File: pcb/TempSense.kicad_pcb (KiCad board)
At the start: 2 copper layers, 90 x 40 mm, 6 parts, among them SW1 Slide_Switch_DPDT_ON-ON_0.3A/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, U1 DC-DC_Converter_Step-Down_5V_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, U2 NodeMCU_Lua_based_ESP8266, U3 Waterproof_Temperature_Sensor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

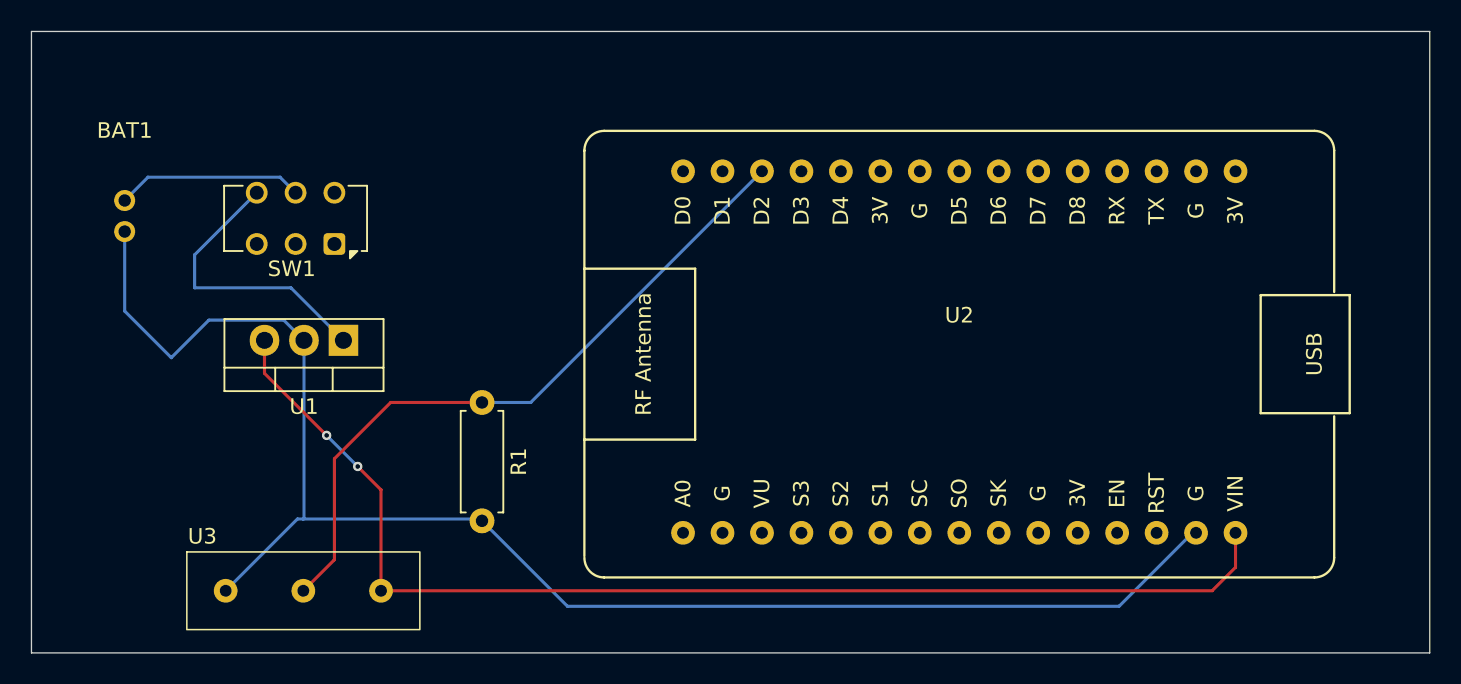
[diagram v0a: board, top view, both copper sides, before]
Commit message: resistor connection corrected to 5V
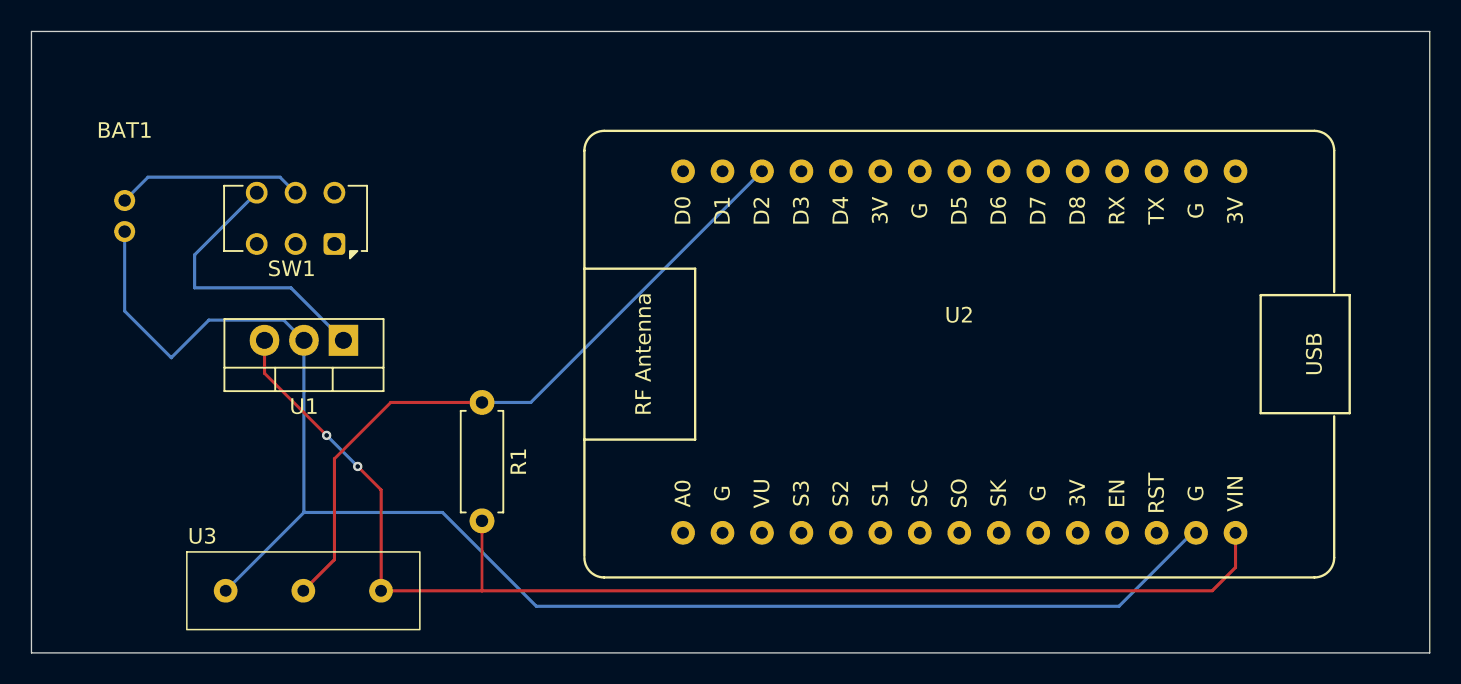
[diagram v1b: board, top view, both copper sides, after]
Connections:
- R1 pad 2: GND -> +5V
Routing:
- net +5V: track 77.1 -> 82.2 mm
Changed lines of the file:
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@@
 			(layers "*.Cu" "*.Mask")
 			(remove_unused_layers no)
-			(net 1 "GND")
+			(net 9 "+5V")
 			(pintype "passive")
 		)
@@
 		(fp_arc
 			(start 14.371974 22.86)
-			(mid 13.999994 23.758021)
+			(mid 13.999993 23.758018)
 			(end 13.101974 24.13)
 			(stroke
@@
 	)
 	(segment
-		(start 105 68.5)
-		(end 104.5 68.5)
+		(start 150.73 69.27)
+		(end 150.96 69.27)
 		(width 0.2)
 		(layer "B.Cu")
@@
 	)
 	(segment
-		(start 105 68.5)
-		(end 110.5 74)
+		(start 93.54 67.96)
+		(end 88.5 73)
+		(width 0.2)
+		(layer "B.Cu")
+		(net 1)
+	)
+	(segment
+		(start 108.5 74)
+		(end 146 74)
+		(width 0.2)
+		(layer "B.Cu")
+		(net 1)
+	)
+	(segment
+		(start 102.46 67.96)
+		(end 108.5 74)
+		(width 0.2)
+		(layer "B.Cu")
+		(net 1)
+	)
+	(segment
+		(start 85 58)
+		(end 87.42 55.58)
+		(width 0.2)
+		(layer "B.Cu")
+		(net 1)
+	)
+	(segment
+		(start 82 55)
+		(end 85 58)
+		(width 0.2)
+		(layer "B.Cu")
+		(net 1)
+	)
+	(segment
+		(start 93.54 67.96)
+		(end 102.46 67.96)
+		(width 0.2)
+		(layer "B.Cu")
+		(net 1)
+	)
+	(segment
+		(start 93.54 56.88)
+		(end 93.54 67.96)
+		(width 0.2)
+		(layer "B.Cu")
+		(net 1)
+	)
+	(segment
+		(start 92.24 55.58)
+		(end 93.54 56.88)
 		(width 0.2)
 		(layer "B.Cu")
@@
 	)
 	(segment
-		(start 85 58)
-		(end 87.42 55.58)
-		(width 0.2)
-		(layer "B.Cu")
-		(net 1)
-	)
-	(segment
-		(start 82 55)
-		(end 85 58)
-		(width 0.2)
-		(layer "B.Cu")
-		(net 1)
-	)
-	(segment
-		(start 110.5 74)
-		(end 146 74)
-		(width 0.2)
-		(layer "B.Cu")
-		(net 1)
-	)
-	(segment
-		(start 104.5 68.5)
-		(end 104.38 68.38)
-		(width 0.2)
-		(layer "B.Cu")
-		(net 1)
-	)
-	(segment
-		(start 93.5 68.38)
-		(end 93.12 68.38)
-		(width 0.2)
-		(layer "B.Cu")
-		(net 1)
-	)
-	(segment
-		(start 92.24 55.58)
-		(end 93.54 56.88)
-		(width 0.2)
-		(layer "B.Cu")
-		(net 1)
-	)
-	(segment
-		(start 104.38 68.38)
-		(end 93.5 68.38)
-		(width 0.2)
-		(layer "B.Cu")
-		(net 1)
-	)
-	(segment
-		(start 93.12 68.38)
-		(end 88.5 73)
-		(width 0.2)
-		(layer "B.Cu")
-		(net 1)
-	)
-	(segment
-		(start 150.73 69.27)
-		(end 150.96 69.27)
-		(width 0.2)
-		(layer "B.Cu")
-		(net 1)
-	)
-	(segment
-		(start 93.54 56.88)
-		(end 93.54 68.34)
-		(width 0.2)
-		(layer "B.Cu")
-		(net 1)
-	)
-	(segment
 		(start 87.42 55.58)
 		(end 92.24 55.58)
@@
 	)
 	(segment
-		(start 93.54 68.34)
-		(end 93.5 68.38)
-		(width 0.2)
-		(layer "B.Cu")
-		(net 1)
-	)
-	(segment
 		(start 82 47.88)
 		(end 83.5 46.38)
@@
 	)
 	(segment
+		(start 152 73)
+		(end 105 73)
+		(width 0.2)
+		(layer "F.Cu")
+		(net 9)
+	)
+	(segment
 		(start 95 63)
 		(end 91 59)
@@
 	)
 	(segment
-		(start 152 73)
-		(end 98.5 73)
+		(start 98.5 73)
+		(end 98.5 66.5)
 		(width 0.2)
 		(layer "F.Cu")
@@
 	)
 	(segment
-		(start 98.5 73)
-		(end 98.5 66.5)
+		(start 105 68.5)
+		(end 105 73)
+		(width 0.2)
+		(layer "F.Cu")
+		(net 9)
+	)
+	(segment
+		(start 105 73)
+		(end 98.5 73)
 		(width 0.2)
 		(layer "F.Cu")
@@
 		(net 9)
 	)
+	(segment
+		(start 105 68.5)
+		(end 104.5 68.5)
+		(width 0.2)
+		(layer "B.Cu")
+		(net 9)
+	)
+	(segment
+		(start 104.5 68.5)
+		(end 104.38 68.38)
+		(width 0.2)
+		(layer "B.Cu")
+		(net 9)
+	)
